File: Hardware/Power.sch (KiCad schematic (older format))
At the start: 11 parts, among them U601 PAM2306AYPAA, U602 PAM2306AYPAA, U603 LDO-X2SON-1.2V, U604 LDO-X2SON-3.3V, U605 LDO-X2SON-2.5V

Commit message: Adding in some power circuitry.
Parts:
- removed U602: PAM2306AYPAA, Package_DFN_QFN:WDFN-12-1EP_3x3mm_P0.45mm_EP1.7x2.5mm, symbol Regulator_Switching:PAM2306AYPAA
- added D?: RB496EATR, Package_TO_SOT_SMD:SOT-23-5, symbol OHMC2022:RB496EATR
- U601: DPN (none) -> PAM2306AYPAADICT-ND; MPN (none) -> PAM2306AYPAA

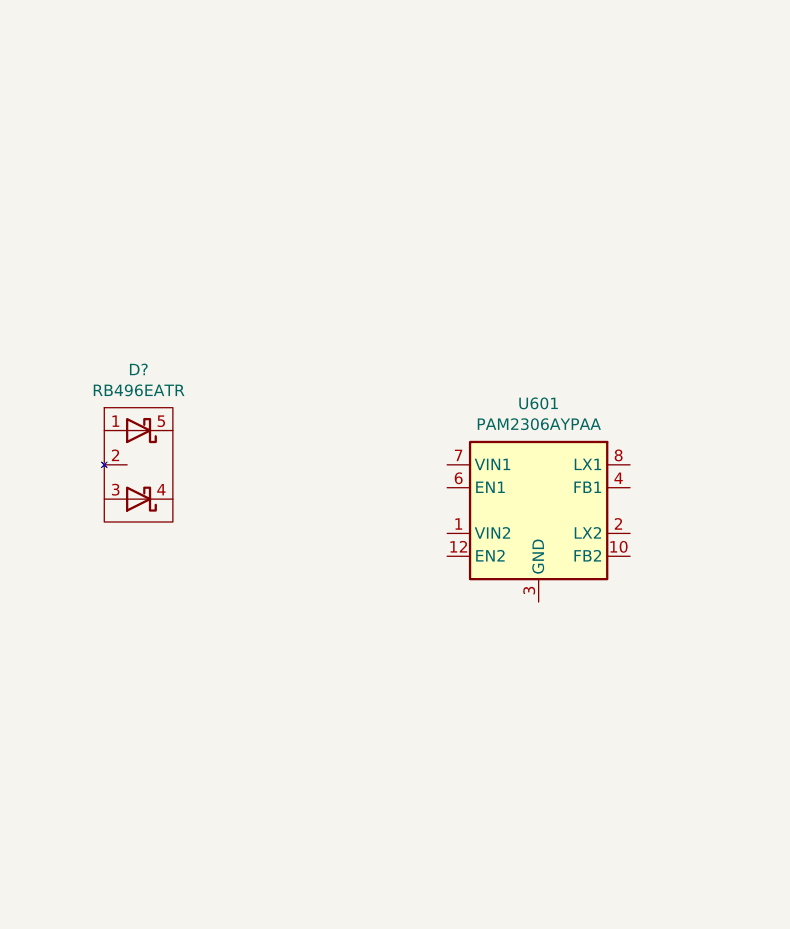
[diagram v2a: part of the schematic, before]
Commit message: Now putting in power and passives.
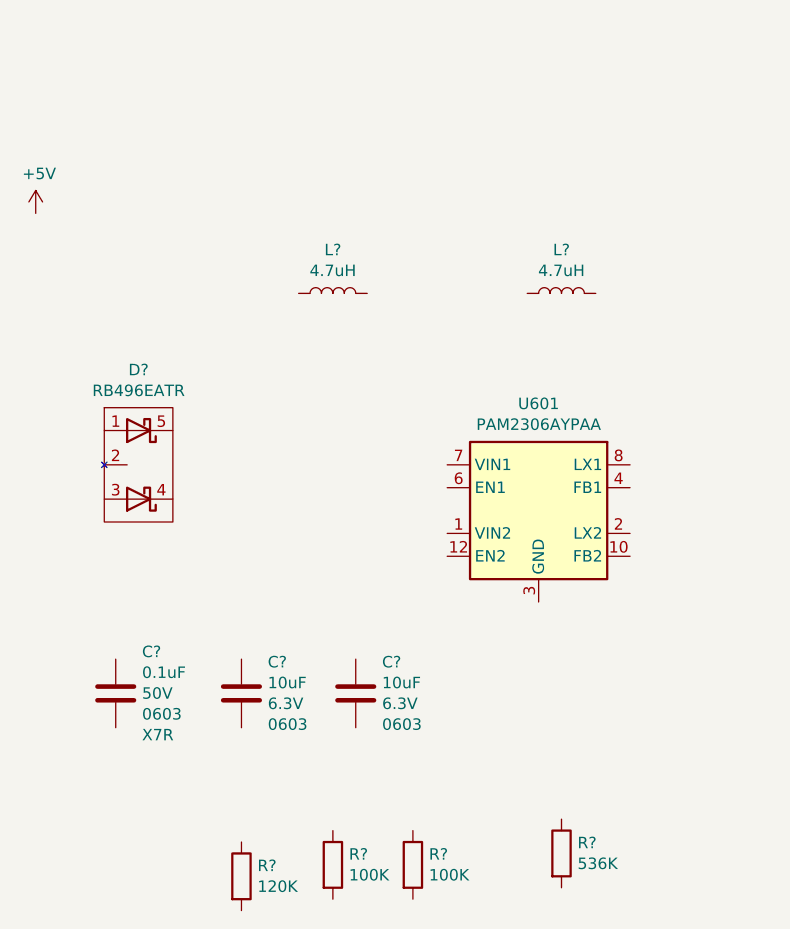
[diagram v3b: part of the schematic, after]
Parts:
- added C? (x2): 10uF, Capacitor_SMD:C_0603_1608Metric, symbol Device:C
- added C?: 0.1uF, Capacitor_SMD:C_0603_1608Metric, symbol Device:C
- added L? (x2): 4.7uH, OHMC2022:SRN4018-4R7M, symbol OHMC2022:Ind-SRN4018
- added R?: 536K, Resistor_SMD:R_0603_1608Metric, symbol Device:R
- added R? (x2): 100K, Resistor_SMD:R_0603_1608Metric, symbol Device:R
- added R?: 120K, Resistor_SMD:R_0603_1608Metric, symbol Device:R
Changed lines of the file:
@@
 EndData
 $EndBitmap
+$Comp
+L OHMC2022:Ind-SRN4018 L?
+U 1 1 612CEAFC
+P 2850 2850
+F 0 "L?" V 3040 2850 50  0000 C CNN
+F 1 "4.7uH" V 2949 2850 50  0000 C CNN
+F 2 "OHMC2022:SRN4018-4R7M" H 2850 2850 50  0001 C CNN
+F 3 "https://www.bourns.com/docs/Product-Datasheets/SRN4018.pdf" H 2850 2850 50  0001 C CNN
+F 4 "SRN4018-4R7M" V 2850 2850 50  0001 C CNN "MPN"
+F 5 "SRN4018-4R7MCT-ND" V 2850 2850 50  0001 C CNN "DPN"
+	1    2850 2850
+	0    -1   -1   0
+$EndComp
+$Comp
+L OHMC2022:Ind-SRN4018 L?
+U 1 1 612D1BE0
+P 3850 2850
+F 0 "L?" V 4040 2850 50  0000 C CNN
+F 1 "4.7uH" V 3949 2850 50  0000 C CNN
+F 2 "OHMC2022:SRN4018-4R7M" H 3850 2850 50  0001 C CNN
+F 3 "https://www.bourns.com/docs/Product-Datasheets/SRN4018.pdf" H 3850 2850 50  0001 C CNN
+F 4 "SRN4018-4R7M" V 3850 2850 50  0001 C CNN "MPN"
+F 5 "SRN4018-4R7MCT-ND" V 3850 2850 50  0001 C CNN "DPN"
+	1    3850 2850
+	0    -1   -1   0
+$EndComp
+$Comp
+L Device:C C?
+U 1 1 612D586D
+P 2450 4600
+F 0 "C?" H 2565 4737 50  0000 L CNN
+F 1 "10uF" H 2565 4646 50  0000 L CNN
+F 2 "Capacitor_SMD:C_0603_1608Metric" H 2488 4450 50  0001 C CNN
+F 3 "~" H 2450 4600 50  0001 C CNN
+F 4 "GRM188R60J106ME47D" H 2450 4600 50  0001 C CNN "MPN"
+F 5 "490-3896-1-ND" H 2450 4600 50  0001 C CNN "DPN"
+F 6 "6.3V" H 2565 4555 50  0000 L CNN "Tol"
+F 7 "0603" H 2565 4464 50  0000 L CNN "Pkg"
+	1    2450 4600
+	1    0    0    -1
+$EndComp
+$Comp
+L Device:C C?
+U 1 1 612D6875
+P 2950 4600
+F 0 "C?" H 3065 4737 50  0000 L CNN
+F 1 "10uF" H 3065 4646 50  0000 L CNN
+F 2 "Capacitor_SMD:C_0603_1608Metric" H 2988 4450 50  0001 C CNN
+F 3 "~" H 2950 4600 50  0001 C CNN
+F 4 "GRM188R60J106ME47D" H 2950 4600 50  0001 C CNN "MPN"
+F 5 "490-3896-1-ND" H 2950 4600 50  0001 C CNN "DPN"
+F 6 "6.3V" H 3065 4555 50  0000 L CNN "Tol"
+F 7 "0603" H 3065 4464 50  0000 L CNN "Pkg"
+	1    2950 4600
+	1    0    0    -1
+$EndComp
+$Comp
+L Device:R R?
+U 1 1 612D860B
+P 3850 5300
+F 0 "R?" H 3920 5346 50  0000 L CNN
+F 1 "536K" H 3920 5255 50  0000 L CNN
+F 2 "Resistor_SMD:R_0603_1608Metric" V 3780 5300 50  0001 C CNN
+F 3 "~" H 3850 5300 50  0001 C CNN
+F 4 "0603" H 3850 5300 50  0001 C CNN "Pkg"
+F 5 "RC0603FR-07536KL" H 3850 5300 50  0001 C CNN "MPN"
+F 6 "311-536KHRCT-ND" H 3850 5300 50  0001 C CNN "DPN"
+	1    3850 5300
+	1    0    0    -1
+$EndComp
+$Comp
+L Device:R R?
+U 1 1 612D89D6
+P 3200 5350
+F 0 "R?" H 3270 5396 50  0000 L CNN
+F 1 "100K" H 3270 5305 50  0000 L CNN
+F 2 "Resistor_SMD:R_0603_1608Metric" V 3130 5350 50  0001 C CNN
+F 3 "~" H 3200 5350 50  0001 C CNN
+F 4 "0603" H 3200 5350 50  0001 C CNN "Pkg"
+F 5 "ESR03EZPJ104" H 3200 5350 50  0001 C CNN "MPN"
+F 6 "RHM100KDCT-ND" H 3200 5350 50  0001 C CNN "DPN"
+	1    3200 5350
+	1    0    0    -1
+$EndComp
+$Comp
+L Device:R R?
+U 1 1 612D8F67
+P 2850 5350
+F 0 "R?" H 2920 5396 50  0000 L CNN
+F 1 "100K" H 2920 5305 50  0000 L CNN
+F 2 "Resistor_SMD:R_0603_1608Metric" V 2780 5350 50  0001 C CNN
+F 3 "~" H 2850 5350 50  0001 C CNN
+F 4 "0603" H 2850 5350 50  0001 C CNN "Pkg"
+F 5 "ESR03EZPJ104" H 2850 5350 50  0001 C CNN "MPN"
+F 6 "RHM100KDCT-ND" H 2850 5350 50  0001 C CNN "DPN"
+	1    2850 5350
+	1    0    0    -1
+$EndComp
+$Comp
+L Device:R R?
+U 1 1 612DA096
+P 2450 5400
+F 0 "R?" H 2520 5446 50  0000 L CNN
+F 1 "120K" H 2520 5355 50  0000 L CNN
+F 2 "Resistor_SMD:R_0603_1608Metric" V 2380 5400 50  0001 C CNN
+F 3 "~" H 2450 5400 50  0001 C CNN
+F 4 "0603" H 2450 5400 50  0001 C CNN "Pkg"
+F 5 "RC0603JR-07120KL" H 2450 5400 50  0001 C CNN "MPN"
+F 6 "311-120KGRCT-ND" H 2450 5400 50  0001 C CNN "DPN"
+	1    2450 5400
+	1    0    0    -1
+$EndComp
+$Comp
+L power:+5V #PWR?
+U 1 1 612DC08D
+P 1550 2500
+AR Path="/6123BB15/612DC08D" Ref="#PWR?"  Part="1"
+AR Path="/611E335F/612DC08D" Ref="#PWR?"  Part="1"
+F 0 "#PWR?" H 1550 2350 50  0001 C CNN
+F 1 "+5V" H 1565 2673 50  0000 C CNN
+F 2 "" H 1550 2500 50  0001 C CNN
+F 3 "" H 1550 2500 50  0001 C CNN
+	1    1550 2500
+	1    0    0    -1
+$EndComp
+$Comp
+L Device:C C?
+U 1 1 612DD1F9
+P 1900 4600
+F 0 "C?" H 2015 4782 50  0000 L CNN
+F 1 "0.1uF" H 2015 4691 50  0000 L CNN
+F 2 "Capacitor_SMD:C_0603_1608Metric" H 1938 4450 50  0001 C CNN
+F 3 "~" H 1900 4600 50  0001 C CNN
+F 4 "C0603C104K5RACAUTO" H 1900 4600 50  0001 C CNN "MPN"
+F 5 "399-6856-1-ND" H 1900 4600 50  0001 C CNN "DPN"
+F 6 "50V" H 2015 4600 50  0000 L CNN "Tol"
+F 7 "0603" H 2015 4509 50  0000 L CNN "Pkg"
+F 8 "X7R" H 2015 4418 50  0000 L CNN "TCoff"
+	1    1900 4600
+	1    0    0    -1
+$EndComp
 $EndSCHEMATC

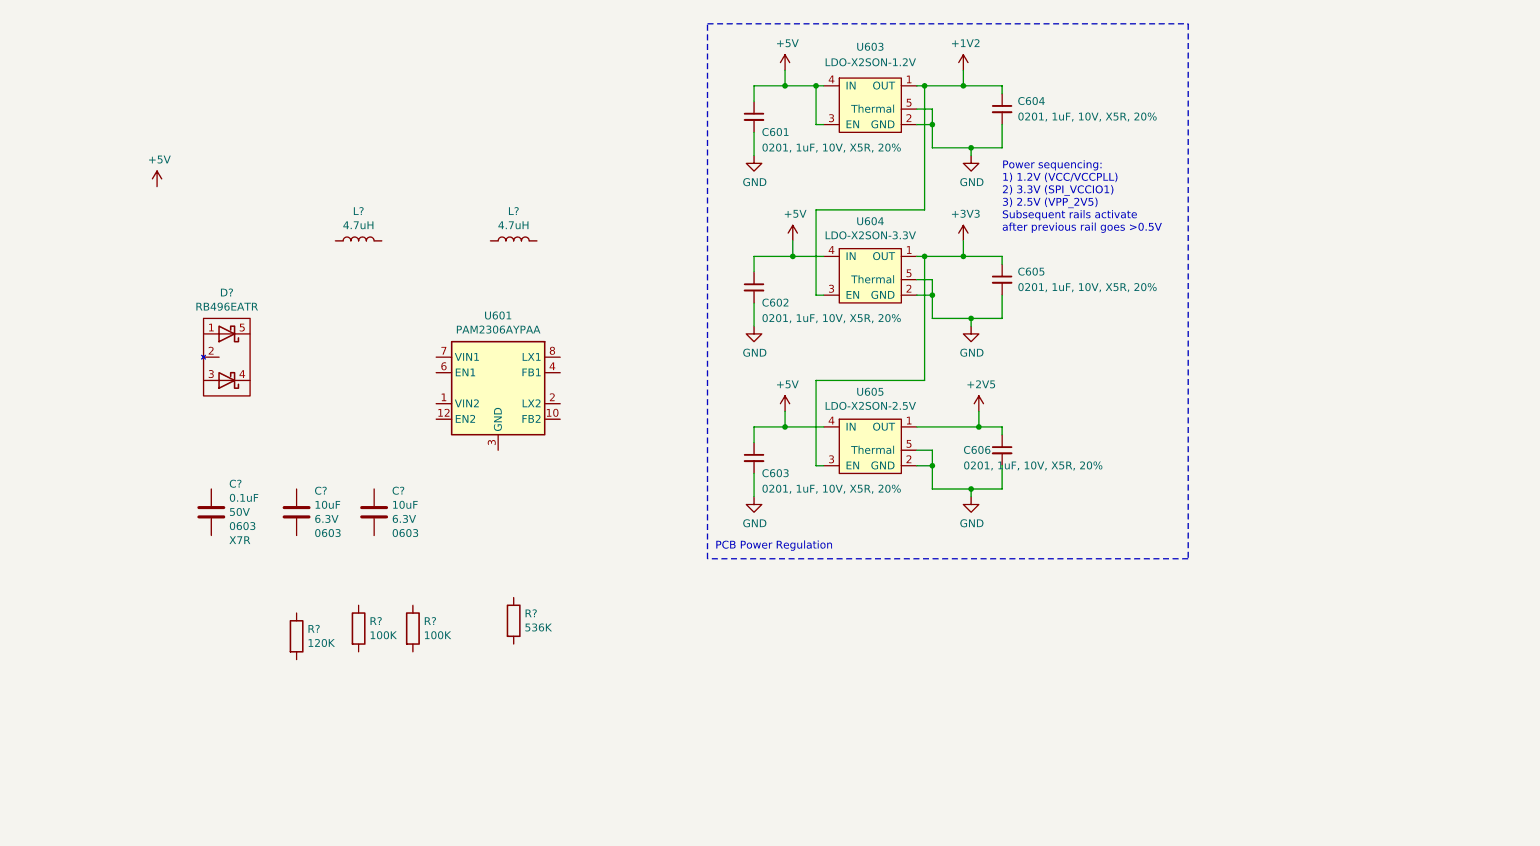
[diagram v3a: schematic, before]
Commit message: Adding in a little more on the power circuitry, vreg for 2v5 rail.
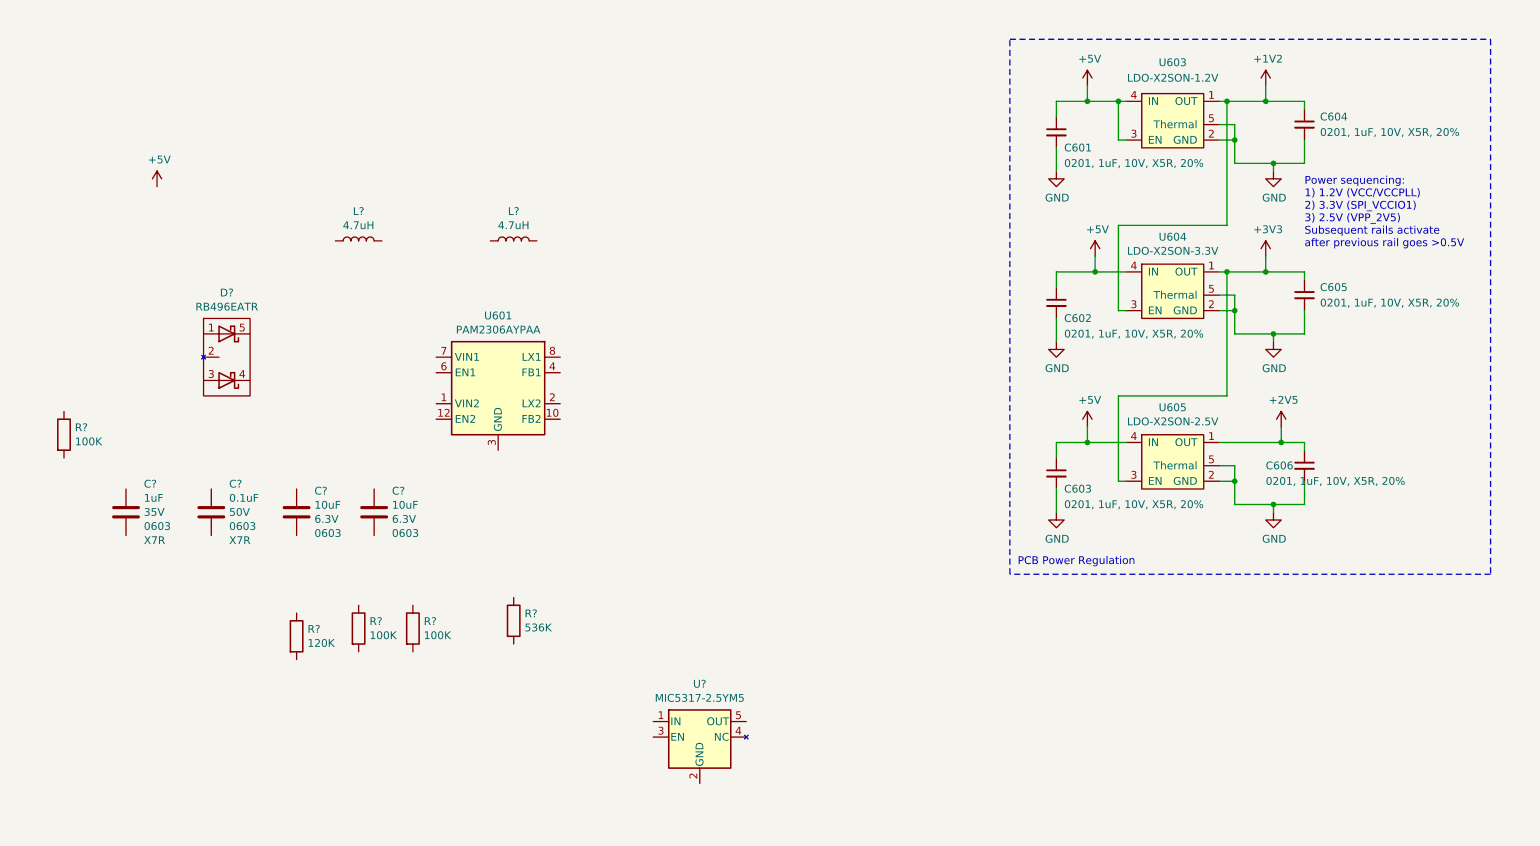
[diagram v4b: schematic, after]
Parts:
- added C?: 1uF, Capacitor_SMD:C_0603_1608Metric, symbol Device:C
- added R?: 100K, Resistor_SMD:R_0603_1608Metric, symbol Device:R
- added U?: MIC5317-2.5YM5, Package_TO_SOT_SMD:SOT-23-5, symbol OHMC2022:MIC5317-2.5YM5
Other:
- moved on the sheet: C601, C602, C603, C604, C605, C606, U603, U604, U605

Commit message: We're going to need a bigger boat.
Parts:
- added R?: 0R, Resistor_SMD:R_0603_1608Metric, symbol Device:R_Small
- R? (x5): symbol Device:R -> Device:R_US
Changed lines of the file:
@@
 $EndComp
 $Comp
-L Device:R R?
+L Device:R_US R?
 U 1 1 612D860B
 P 3850 5300
-F 0 "R?" H 3920 5346 50  0000 L CNN
-F 1 "536K" H 3920 5255 50  0000 L CNN
+F 0 "R?" H 3918 5346 50  0000 L CNN
+F 1 "536K" H 3918 5255 50  0000 L CNN
 F 2 "Resistor_SMD:R_0603_1608Metric" V 3780 5300 50  0001 C CNN
 F 3 "~" H 3850 5300 50  0001 C CNN
@@
 $EndComp
 $Comp
-L Device:R R?
+L Device:R_US R?
 U 1 1 612D89D6
 P 3200 5350
-F 0 "R?" H 3270 5396 50  0000 L CNN
-F 1 "100K" H 3270 5305 50  0000 L CNN
+F 0 "R?" H 3268 5396 50  0000 L CNN
+F 1 "100K" H 3268 5305 50  0000 L CNN
 F 2 "Resistor_SMD:R_0603_1608Metric" V 3130 5350 50  0001 C CNN
 F 3 "~" H 3200 5350 50  0001 C CNN
@@
 $EndComp
 $Comp
-L Device:R R?
+L Device:R_US R?
 U 1 1 612D8F67
 P 2850 5350
-F 0 "R?" H 2920 5396 50  0000 L CNN
-F 1 "100K" H 2920 5305 50  0000 L CNN
+F 0 "R?" H 2918 5396 50  0000 L CNN
+F 1 "100K" H 2918 5305 50  0000 L CNN
 F 2 "Resistor_SMD:R_0603_1608Metric" V 2780 5350 50  0001 C CNN
 F 3 "~" H 2850 5350 50  0001 C CNN
@@
 $EndComp
 $Comp
-L Device:R R?
+L Device:R_US R?
 U 1 1 612DA096
 P 2450 5400
-F 0 "R?" H 2520 5446 50  0000 L CNN
-F 1 "120K" H 2520 5355 50  0000 L CNN
+F 0 "R?" H 2518 5446 50  0000 L CNN
+F 1 "120K" H 2518 5355 50  0000 L CNN
 F 2 "Resistor_SMD:R_0603_1608Metric" V 2380 5400 50  0001 C CNN
 F 3 "~" H 2450 5400 50  0001 C CNN
@@
 F 6 "311-120KGRCT-ND" H 2450 5400 50  0001 C CNN "DPN"
 	1    2450 5400
-	1    0    0    -1
-$EndComp
-$Comp
-L power:+5V #PWR?
-U 1 1 612DC08D
-P 1550 2500
-AR Path="/6123BB15/612DC08D" Ref="#PWR?"  Part="1"
-AR Path="/611E335F/612DC08D" Ref="#PWR?"  Part="1"
-F 0 "#PWR?" H 1550 2350 50  0001 C CNN
-F 1 "+5V" H 1565 2673 50  0000 C CNN
-F 2 "" H 1550 2500 50  0001 C CNN
-F 3 "" H 1550 2500 50  0001 C CNN
-	1    1550 2500
 	1    0    0    -1
 $EndComp
@@
 $EndComp
 $Comp
-L Device:R R?
+L Device:R_US R?
 U 1 1 612EE9BF
 P 950 4100
-F 0 "R?" H 1020 4146 50  0000 L CNN
-F 1 "100K" H 1020 4055 50  0000 L CNN
+F 0 "R?" H 1018 4146 50  0000 L CNN
+F 1 "100K" H 1018 4055 50  0000 L CNN
 F 2 "Resistor_SMD:R_0603_1608Metric" V 880 4100 50  0001 C CNN
 F 3 "~" H 950 4100 50  0001 C CNN
@@
 	1    0    0    -1
 $EndComp
+$Comp
+L power:+5V #PWR?
+U 1 1 612F5A7F
+P 2650 1600
+AR Path="/6123BB15/612F5A7F" Ref="#PWR?"  Part="1"
+AR Path="/611E335F/612F5A7F" Ref="#PWR?"  Part="1"
+F 0 "#PWR?" H 2650 1450 50  0001 C CNN
+F 1 "+5V" H 2665 1773 50  0000 C CNN
+F 2 "" H 2650 1600 50  0001 C CNN
+F 3 "" H 2650 1600 50  0001 C CNN
+	1    2650 1600
+	1    0    0    -1
+$EndComp
+$Comp
+L Device:R_Small R?
+U 1 1 612F9833
+P 1000 3350
+F 0 "R?" H 1059 3396 50  0000 L CNN
+F 1 "0R" H 1059 3305 50  0000 L CNN
+F 2 "Resistor_SMD:R_0603_1608Metric" V 930 3350 50  0001 C CNN
+F 3 "~" H 1000 3350 50  0001 C CNN
+F 4 "0603" H 1000 3350 50  0001 C CNN "Pkg"
+F 5 "RC0603JR-070RL" H 1000 3350 50  0001 C CNN "MPN"
+F 6 "311-0.0GRCT-ND" H 1000 3350 50  0001 C CNN "DPN"
+	1    1000 3350
+	1    0    0    -1
+$EndComp
